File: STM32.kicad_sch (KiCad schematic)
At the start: 42 parts, among them IC201 ESDALC6V1W5, IC202 ESDALC6V1W5, IC203 ESDALC6V1W5, J206 Conn_01x04_Pin, J207 Conn_01x07_Pin, Q201 DMG1012T-13, Q202 DMG1012T-13, Q203 DMG1012T-13, Q204 DMG1012T-13, U201 TLV9304IDR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

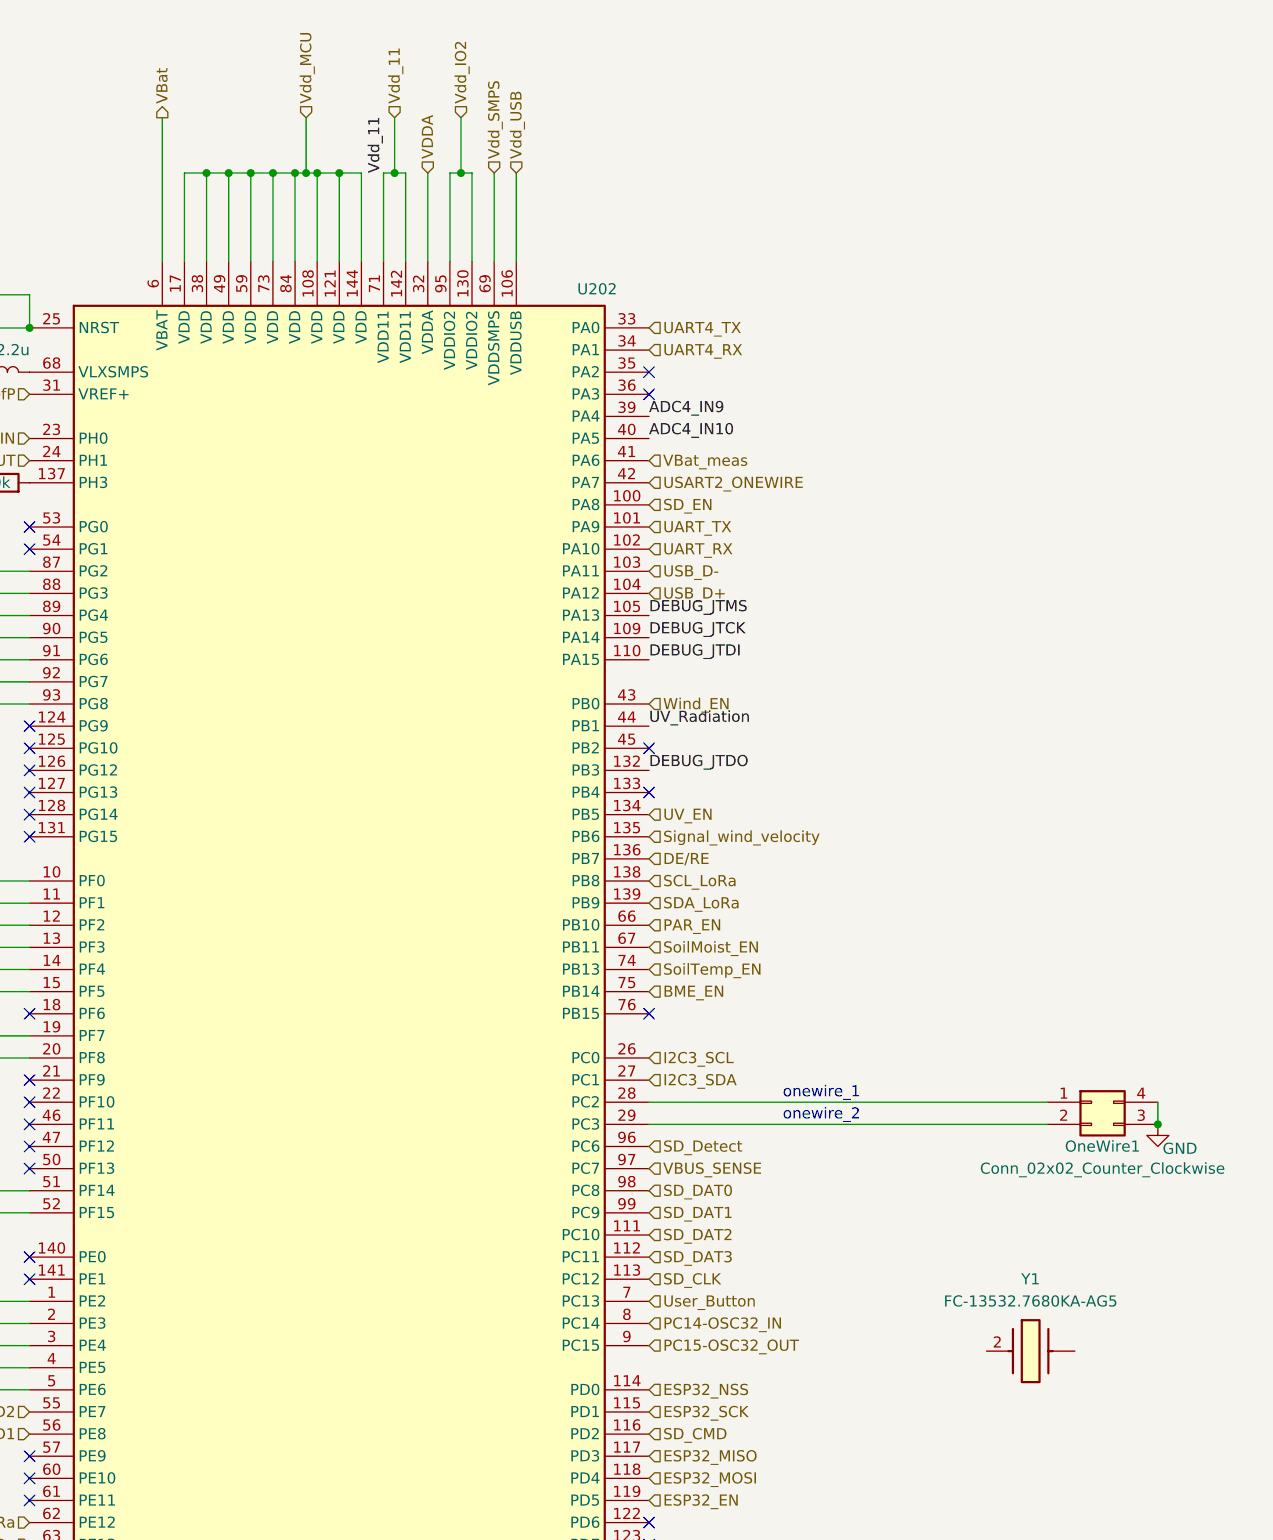
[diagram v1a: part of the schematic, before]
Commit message: Add TP4056-18650 footprint and update Power schematic
Added the TP4056-18650-2 footprint to the library and assigned it to the battery charger in Power.kicad_sch. Updated the Power schematic to improve symbol details, add descriptive properties, and enhance the 3V3 lane toggling section. Made various net and annotation adjustments, and removed obsolete autosave and lock files.
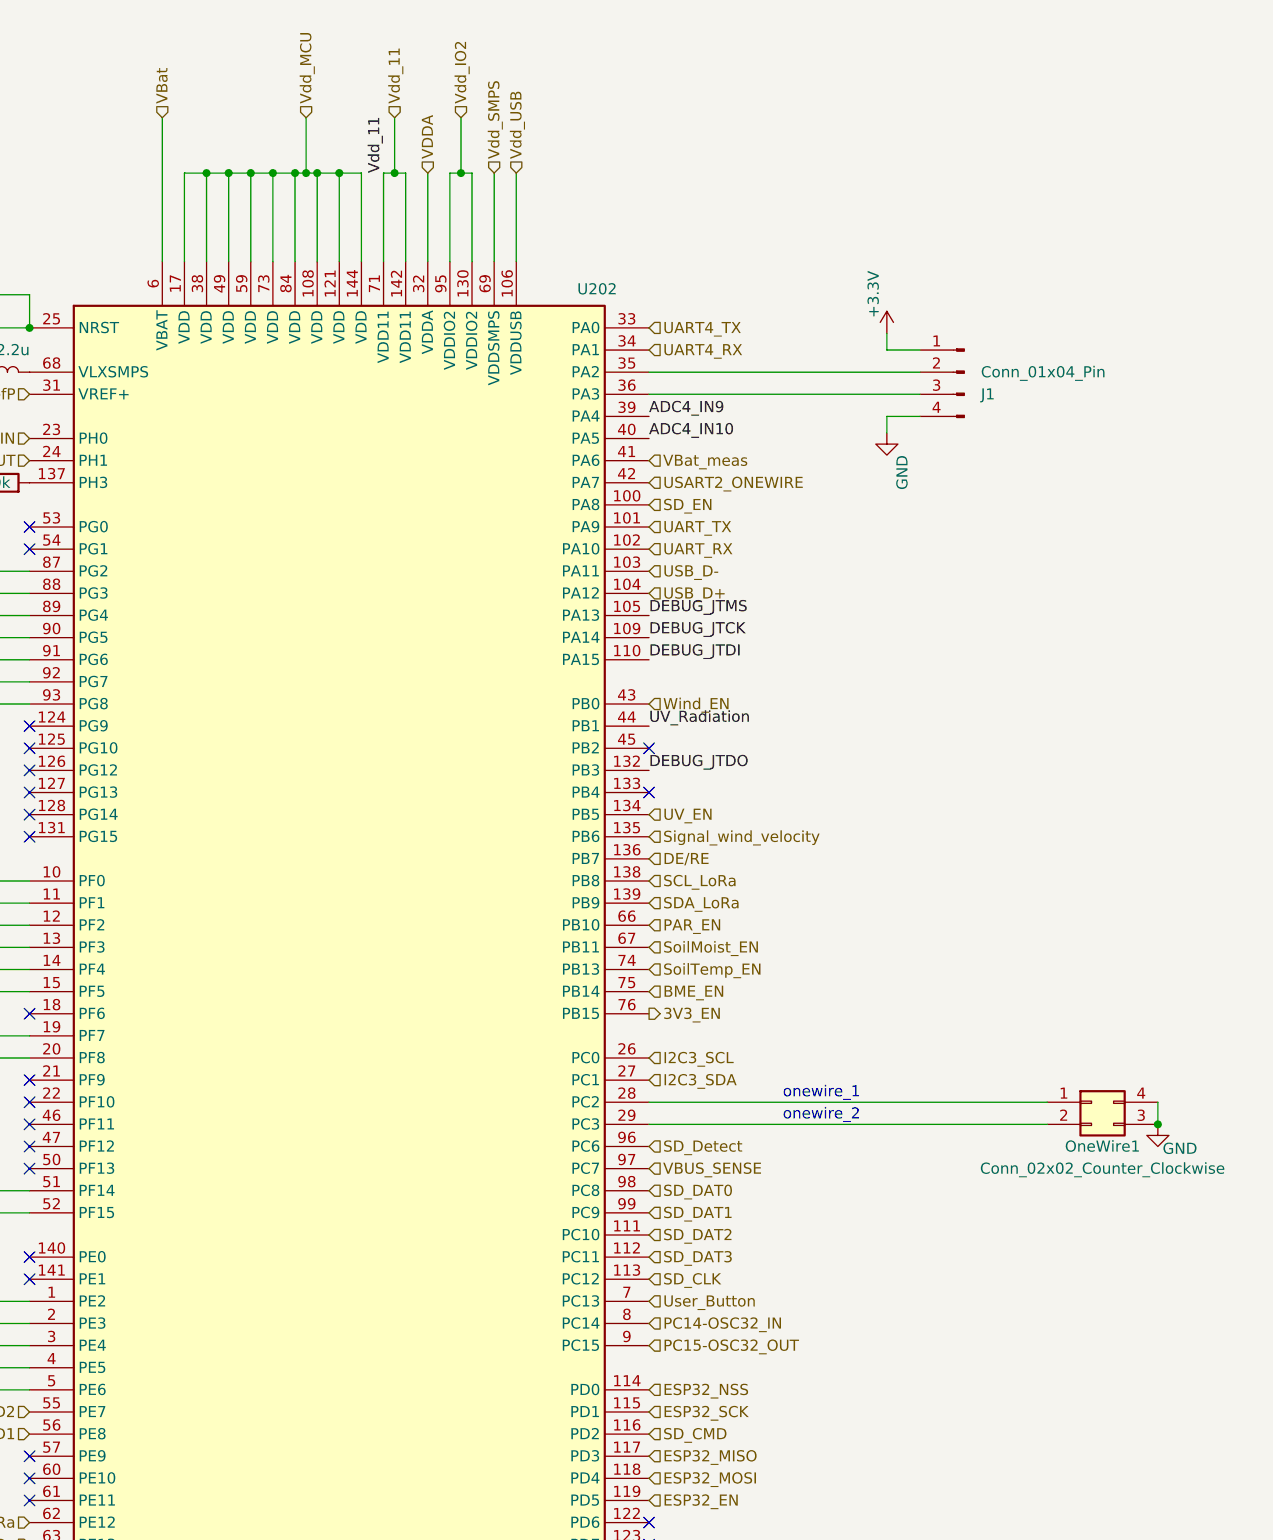
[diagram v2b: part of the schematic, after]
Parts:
- removed Y1: FC-13532.7680KA-AG5, FC135327680KAAG5, symbol SamacSys_Parts:FC-13532.7680KA-AG5
- added J1: Conn_01x04_Pin, Connector_PinHeader_2.54mm:PinHeader_1x04_P2.54mm_Vertical, symbol Connector:Conn_01x04_Pin
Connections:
- net +3.3V: now also J1.1 (Pin_1)
- net GND: now also J1.4 (Pin_4)
- net at U202.35 (PA2): now also J1.2 (Pin_2)
- net at U202.36 (PA3): now also J1.3 (Pin_3)
- net 3V3_EN: now reaches U202.76 (PB15)
- no-connect marks 35 -> 32
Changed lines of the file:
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@@
 	)
 	(no_connect
-		(at 215.9 91.44)
-	)
-	(no_connect
 		(at 39.37 171.45)
 	)
@@
 	)
 	(no_connect
-		(at 215.9 88.9)
-	)
-	(no_connect
 		(at 215.9 137.16)
 	)
@@
 	)
 	(no_connect
-		(at 215.9 162.56)
-	)
-	(no_connect
 		(at 215.9 233.68)
 	)
@@
 	(wire
 		(pts
+			(xy 215.9 91.44) (xy 247.015 91.44)
+		)
+		(stroke
+			(width 0)
+			(type default)
+		)
+	)
+	(wire
+		(pts
 			(xy 185.42 66.04) (xy 186.69 66.04)
 		)
@@
 	(wire
 		(pts
+			(xy 215.9 88.9) (xy 247.015 88.9)
+		)
+		(stroke
+			(width 0)
+			(type default)
+		)
+	)
+	(wire
+		(pts
 			(xy 166.37 254) (xy 166.37 264.16)
 		)
@@
 	(wire
 		(pts
+			(xy 247.015 93.98) (xy 243.205 93.98)
+		)
+		(stroke
+			(width 0)
+			(type default)
+		)
+	)
+	(wire
+		(pts
 			(xy 175.26 66.04) (xy 176.53 66.04)
 		)
@@
 	(wire
 		(pts
+			(xy 243.205 86.36) (xy 247.015 86.36)
+		)
+		(stroke
+			(width 0)
+			(type default)
+		)
+	)
+	(wire
+		(pts
 			(xy 167.64 66.04) (xy 170.18 66.04)
 		)
@@
 	(wire
 		(pts
+			(xy 243.205 93.98) (xy 243.205 95.885)
+		)
+		(stroke
+			(width 0)
+			(type default)
+		)
+	)
+	(wire
+		(pts
 			(xy 144.78 80.01) (xy 144.78 83.82)
 		)
@@
 	(wire
 		(pts
+			(xy 243.205 84.455) (xy 243.205 86.36)
+		)
+		(stroke
+			(width 0)
+			(type default)
+		)
+	)
+	(wire
+		(pts
 			(xy 137.16 302.26) (xy 137.16 304.8)
 		)
@@
 		)
 	)
+	(hierarchical_label "3V3_EN"
+		(shape output)
+		(at 215.9 162.56 0)
+		(effects
+			(font
+				(size 1.27 1.27)
+			)
+			(justify left)
+		)
+	)
 	(hierarchical_label "I2C3_SCL"
 		(shape input)
@@
 	)
 	(hierarchical_label "VBat"
-		(shape output)
+		(shape input)
 		(at 160.02 59.69 90)
 		(effects
@@
 	)
 	(symbol
+		(lib_id "power:GND")
+		(at 243.205 95.885 0)
+		(unit 1)
+		(exclude_from_sim no)
+		(in_bom yes)
+		(on_board yes)
+		(dnp no)
+		(property "Reference" "#PWR025"
+			(at 243.205 102.235 0)
+			(effects
+				(font
+					(size 1.27 1.27)
+				)
+				(hide yes)
+			)
+		)
+		(property "Value" "GND"
+			(at 244.983 98.425 90)
+			(effects
+				(font
+					(size 1.27 1.27)
+				)
+				(justify right)
+			)
+		)
+		(property "Footprint" ""
+			(at 243.205 95.885 0)
+			(effects
+				(font
+					(size 1.27 1.27)
+				)
+				(hide yes)
+			)
+		)
+		(property "Datasheet" ""
+			(at 243.205 95.885 0)
+			(effects
+				(font
+					(size 1.27 1.27)
+				)
+				(hide yes)
+			)
+		)
+		(property "Description" "Power symbol creates a global label with name \"GND\" , ground"
+			(at 243.205 95.885 0)
+			(effects
+				(font
+					(size 1.27 1.27)
+				)
+				(hide yes)
+			)
+		)
+		(pin "1"
+		)
+		(instances
+			(project "µC_Agri-PV"
+				(path "/69abffa1-550c-4cd8-ae80-a1755923d6dc/68eeaf65-50b7-4f21-91a4-9a8eefc615e6"
+					(reference "#PWR025")
+					(unit 1)
+				)
+			)
+		)
+	)
+	(symbol
 		(lib_id "Device:C")
 		(at 69.85 295.91 270)
@@
 	)
 	(symbol
+		(lib_id "power:+3.3V")
+		(at 243.205 84.455 0)
+		(unit 1)
+		(exclude_from_sim no)
+		(in_bom yes)
+		(on_board yes)
+		(dnp no)
+		(property "Reference" "#PWR024"
+			(at 243.205 88.265 0)
+			(effects
+				(font
+					(size 1.27 1.27)
+				)
+				(hide yes)
+			)
+		)
+		(property "Value" "+3.3V"
+			(at 241.681 82.677 90)
+			(effects
+				(font
+					(size 1.27 1.27)
+				)
+				(justify left)
+			)
+		)
+		(property "Footprint" ""
+			(at 243.205 84.455 0)
+			(effects
+				(font
+					(size 1.27 1.27)
+				)
+				(hide yes)
+			)
+		)
+		(property "Datasheet" ""
+			(at 243.205 84.455 0)
+			(effects
+				(font
+					(size 1.27 1.27)
+				)
+				(hide yes)
+			)
+		)
+		(property "Description" "Power symbol creates a global label with name \"+3.3V\""
+			(at 243.205 84.455 0)
+			(effects
+				(font
+					(size 1.27 1.27)
+				)
+				(hide yes)
+			)
+		)
+		(pin "1"
+		)
+		(instances
+			(project "µC_Agri-PV"
+				(path "/69abffa1-550c-4cd8-ae80-a1755923d6dc/68eeaf65-50b7-4f21-91a4-9a8eefc615e6"
+					(reference "#PWR024")
+					(unit 1)
+				)
+			)
+		)
+	)
+	(symbol
 		(lib_id "Connector:Conn_01x04_Pin")
 		(at 55.88 115.57 0)
@@
 	)
 	(symbol
+		(lib_id "Connector:Conn_01x04_Pin")
+		(at 252.095 88.9 0)
+		(mirror y)
+		(unit 1)
+		(exclude_from_sim no)
+		(in_bom yes)
+		(on_board yes)
+		(dnp no)
+		(fields_autoplaced yes)
+		(property "Reference" "J1"
+			(at 254 91.4401 0)
+			(effects
+				(font
+					(size 1.27 1.27)
+				)
+				(justify right)
+			)
+		)
+		(property "Value" "Conn_01x04_Pin"
+			(at 254 88.9001 0)
+			(effects
+				(font
+					(size 1.27 1.27)
+				)
+				(justify right)
+			)
+		)
+		(property "Footprint" "Connector_PinHeader_2.54mm:PinHeader_1x04_P2.54mm_Vertical"
+			(at 252.095 88.9 0)
+			(effects
+				(font
+					(size 1.27 1.27)
+				)
+				(hide yes)
+			)
+		)
+		(property "Datasheet" "~"
+			(at 252.095 88.9 0)
+			(effects
+				(font
+					(size 1.27 1.27)
+				)
+				(hide yes)
+			)
+		)
+		(property "Description" "Generic connector, single row, 01x04, script generated"
+			(at 252.095 88.9 0)
+			(effects
+				(font
+					(size 1.27 1.27)
+				)
+				(hide yes)
+			)
+		)
+		(pin "3"
+		)
+		(pin "4"
+		)
+		(pin "1"
+		)
+		(pin "2"
+		)
+		(instances
+			(project "µC_Agri-PV"
+				(path "/69abffa1-550c-4cd8-ae80-a1755923d6dc/68eeaf65-50b7-4f21-91a4-9a8eefc615e6"
+					(reference "J1")
+					(unit 1)
+				)
+			)
+		)
+	)
+	(symbol
 		(lib_id "power:+3.3V")
 		(at 125.73 134.62 0)
@@
 					(unit 1)
 				)
-			)
-		)
-	)
-	(symbol
-		(lib_id "SamacSys_Parts:FC-13532.7680KA-AG5")
-		(at 254.635 201.295 0)
-		(unit 1)
-		(exclude_from_sim no)
-		(in_bom yes)
-		(on_board yes)
-		(dnp no)
-		(fields_autoplaced yes)
-		(property "Reference" "Y1"
-			(at 259.715 193.04 0)
-			(effects
-				(font
-					(size 1.27 1.27)
-				)
-			)
-		)
-		(property "Value" "FC-13532.7680KA-AG5"
-			(at 259.715 195.58 0)
-			(effects
-				(font
-					(size 1.27 1.27)
-				)
-			)
-		)
-		(property "Footprint" "FC135327680KAAG5"
-			(at 263.525 297.485 0)
-			(effects
-				(font
-					(size 1.27 1.27)
-				)
-				(justify left top)
-				(hide yes)
-			)
-		)
-		(property "Datasheet" "https://support.epson.biz/td/api/doc_check.php?dl=brief_FC-135&lang=en"
-			(at 263.525 397.485 0)
-			(effects
-				(font
-					(size 1.27 1.27)
-				)
-				(justify left top)
-				(hide yes)
-			)
-		)
-		(property "Description" "32.768kHz +/-20ppm Crystal 7pF 70 kOhms 2-SMD, No Lead"
-			(at 254.635 201.295 0)
-			(effects
-				(font
-					(size 1.27 1.27)
-				)
-				(hide yes)
-			)
-		)
-		(property "Height" "0.9"
-			(at 263.525 597.485 0)
-			(effects
-				(font
-					(size 1.27 1.27)
-				)
-				(justify left top)
-				(hide yes)
-			)
-		)
-		(property "Mouser Part Number" ""
-			(at 263.525 697.485 0)
-			(effects
-				(font
-					(size 1.27 1.27)
-				)
-				(justify left top)
-				(hide yes)
-			)
-		)
-		(property "Mouser Price/Stock" ""
-			(at 263.525 797.485 0)
-			(effects
-				(font
-					(size 1.27 1.27)
-				)
-				(justify left top)
-				(hide yes)
-			)
-		)
-		(property "Manufacturer_Name" "Seiko Epson Corporation"
-			(at 263.525 897.485 0)
-			(effects
-				(font
-					(size 1.27 1.27)
-				)
-				(justify left top)
-				(hide yes)
-			)
-		)
-		(property "Manufacturer_Part_Number" "FC-13532.7680KA-AG5"
-			(at 263.525 997.485 0)
-			(effects
-				(font
-					(size 1.27 1.27)
-				)
-				(justify left top)
-				(hide yes)
-			)
-		)
-		(pin ""
-		)
-		(pin "2"
-		)
-		(instances
-			(project ""
-				(path "/69abffa1-550c-4cd8-ae80-a1755923d6dc/68eeaf65-50b7-4f21-91a4-9a8eefc615e6"
-					(reference "Y1")
-					(unit 1)
-				)
